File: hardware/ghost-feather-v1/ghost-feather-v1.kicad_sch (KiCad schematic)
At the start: 96 parts, among them J1 Conn_ARM_SWD_TagConnect_TC2030, J2 USB_C_Receptacle_USB2.0, J3 Conn_01x03, J4 Conn_01x03, J5 Conn_01x03, J6 Conn_01x03, J7 Conn_01x08, J8 Conn_01x02, Q1 BSS138, Q2 BSS138, Q3 BSS138, Q4 BSS138, SW2 BOOT0, U1 STM32F722RETx, U2 BMI270, U3 USBLC6-2SC6_MOD, U4 MPM3610, U5 MPM3610, X1 16MHz, X2 32kHz768

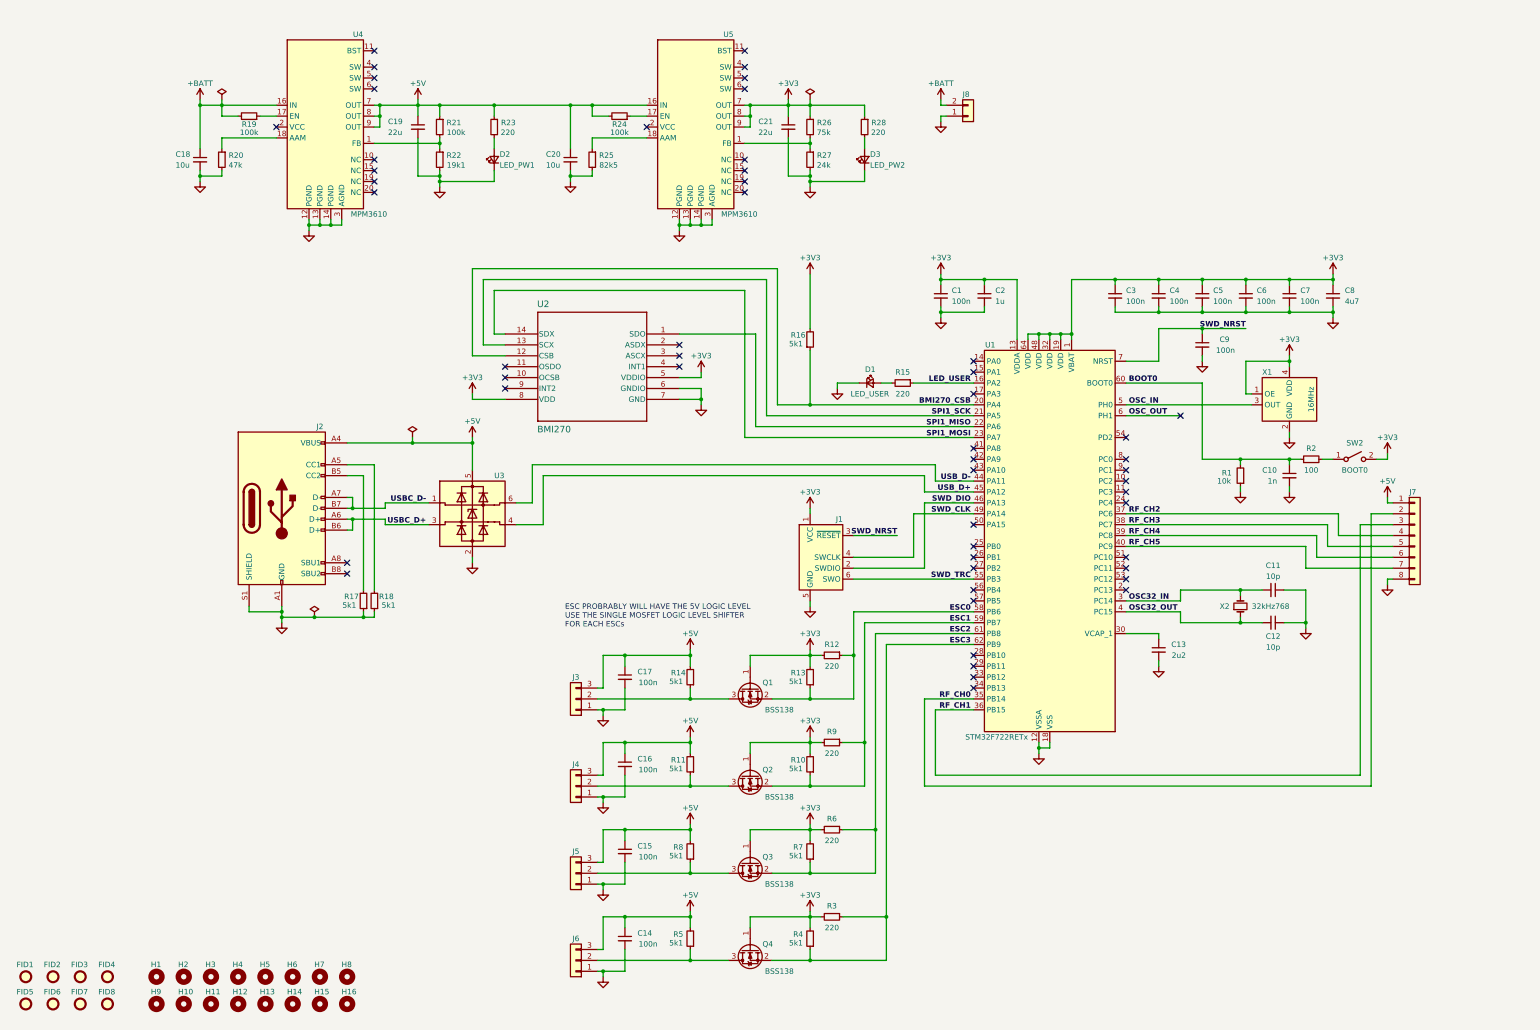
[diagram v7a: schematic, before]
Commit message: feat: Add sections on the schematic
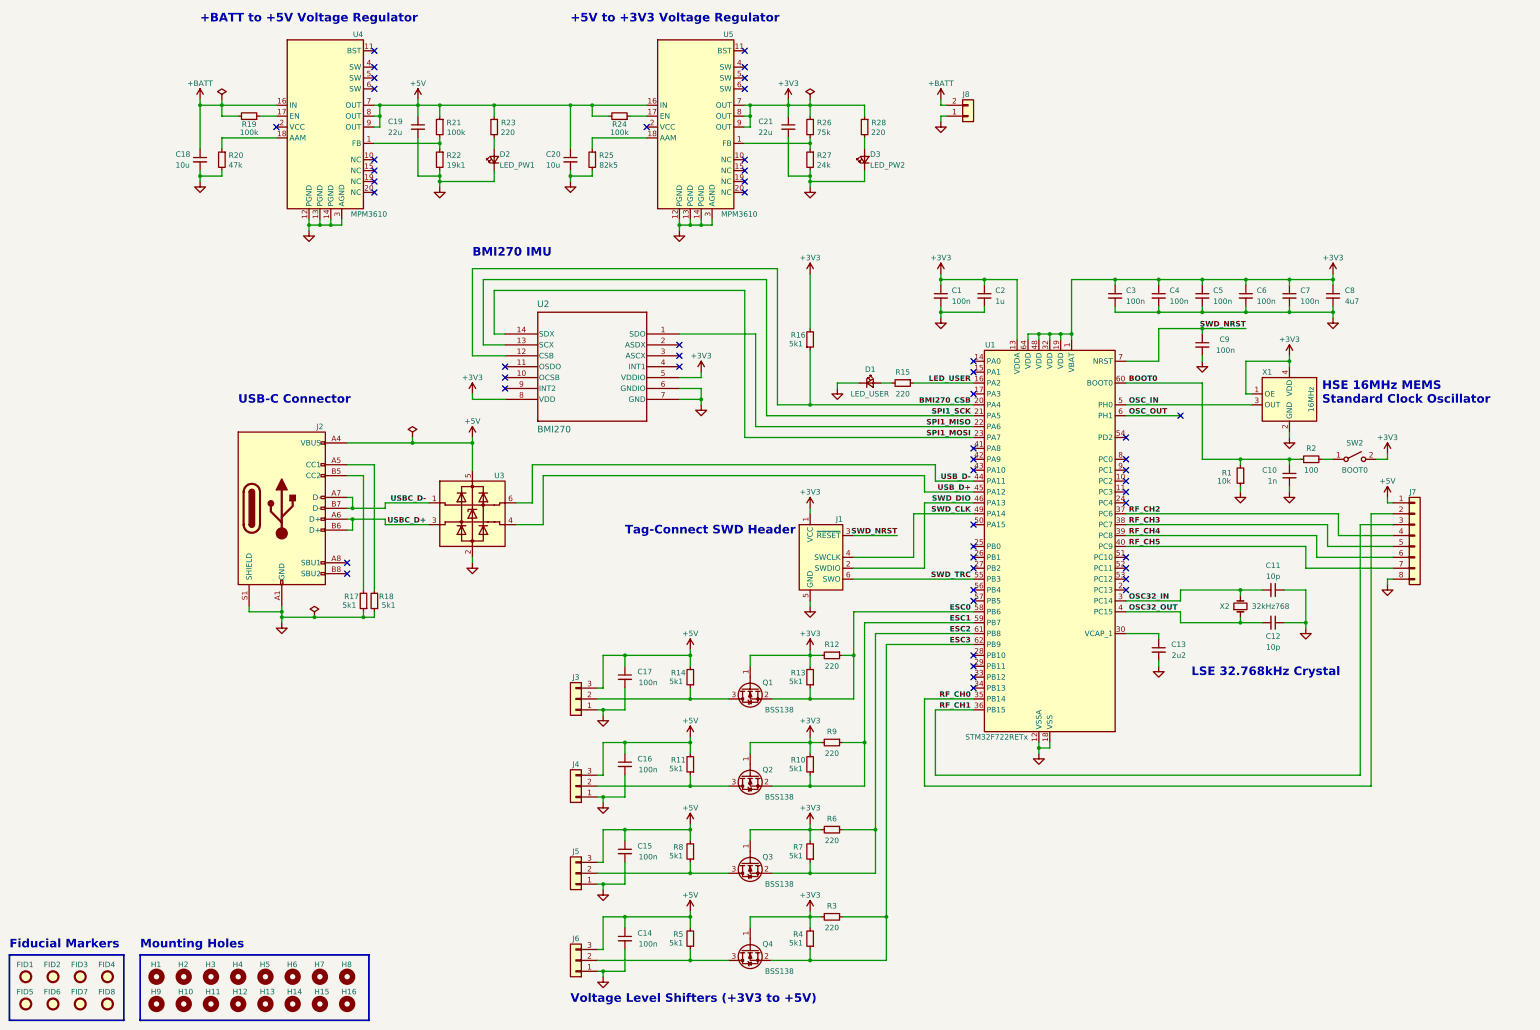
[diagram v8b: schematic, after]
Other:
- note added: "+5V to +3V3 Voltage Regulator"
- note added: "+BATT to +5V Voltage Regulator"
- note added: "BMI270 IMU"
- note added: "Fiducial Markers"
- note added: "HSE 16MHz MEMS Standard Clock Oscillator"
- note added: "LSE 32.768kHz Crystal"
- note added: "Mounting Holes"
- note added: "Tag-Connect SWD Header"
- note added: "USB-C Connector"
- note added: "Voltage Level Shifters (+3V3 to +5V)"
- note removed: "ESC PROBRABLY WILL HAVE THE 5V LOGIC LEVEL USE THE SINGLE MOSFET LOGIC LEVEL SHIFTER FOR EACH ESCs"
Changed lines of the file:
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@@
     (stroke (width 0) (type default))
   )
-  (text "ESC PROBRABLY WILL HAVE THE 5V LOGIC LEVEL\nUSE THE SINGLE MOSFET LOGIC LEVEL SHIFTER\nFOR EACH ESCs\n"
-    (at 160.02 170.18 0)
-    (effects (font (size 1.27 1.27)) (justify left bottom))
+  (rectangle (start 60.96 246.38) (end 114.3 261.62)
+    (stroke (width 0.4) (type default))
+    (fill (type none))
+  )
+  (rectangle (start 30.48 246.38) (end 57.15 261.62)
+    (stroke (width 0.4) (type default))
+    (fill (type none))
+  )
+  (text "HSE 16MHz MEMS\nStandard Clock Oscillator" (at 336.55 118.11 0)
+    (effects (font (size 2 2) (thickness 0.254) bold) (justify left bottom))
+  )
+  (text "Tag-Connect SWD Header" (at 173.99 148.59 0)
+    (effects (font (size 2 2) (thickness 0.254) bold) (justify left bottom))
+  )
+  (text "BMI270 IMU" (at 138.43 83.82 0)
+    (effects (font (size 2 2) (thickness 0.254) bold) (justify left bottom))
+  )
+  (text "LSE 32.768kHz Crystal" (at 306.07 181.61 0)
+    (effects (font (size 2 2) (thickness 0.254) bold) (justify left bottom))
+  )
+  (text "USB-C Connector" (at 83.82 118.11 0)
+    (effects (font (size 2 2) (thickness 0.254) bold) (justify left bottom))
+  )
+  (text "Voltage Level Shifters (+3V3 to +5V)" (at 161.29 257.81 0)
+    (effects (font (size 2 2) (thickness 0.254) bold) (justify left bottom))
+  )
+  (text "+5V to +3V3 Voltage Regulator" (at 161.29 29.21 0)
+    (effects (font (size 2 2) (thickness 0.254) bold) (justify left bottom))
+  )
+  (text "+BATT to +5V Voltage Regulator" (at 74.93 29.21 0)
+    (effects (font (size 2 2) (thickness 0.254) bold) (justify left bottom))
+  )
+  (text "Fiducial Markers" (at 30.48 245.11 0)
+    (effects (font (size 2 2) (thickness 0.254) bold) (justify left bottom))
+  )
+  (text "Mounting Holes" (at 60.96 245.11 0)
+    (effects (font (size 2 2) (thickness 0.254) bold) (justify left bottom))
   )
   (label "BOOT0" (at 291.465 113.03 0) (fields_autoplaced)
